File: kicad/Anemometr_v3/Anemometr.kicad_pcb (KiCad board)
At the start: 2 copper layers, 45 x 45 mm, 131 parts, among them J1 TxD, J10 +Z1, J11 +Z2, J12 +Z3, J13 +Z4, J14 -Z1, J15 -Z2, J16 -Z3, J17 -Z4, J2 RxD, J24 +Z1, J25 +Z1, J26 +Z1, J27 +Z1, J28 +Z1, J29 +Z1, J3 JST-SH1.0, J30 +Z1, J31 +Z1, J32 +Z1, J33 +Z1, J34 +Z1, J35 +Z1, J36 +Z1, J37 +Z1, J38 +Z1, J39 +Z1, J4 JST-SH1.0, J5 RST, J6 +EXT, J7 -EXT, J8 SWD, J9 SWC, Q1 5N10, U1 STM32F103C8Tx, U4 LMR14206, U6 NCP1117-3.3, U9 MCP1703-3.3, Y1 CSTCE8M00G52A-R0, Y2 ECS-250-20-33

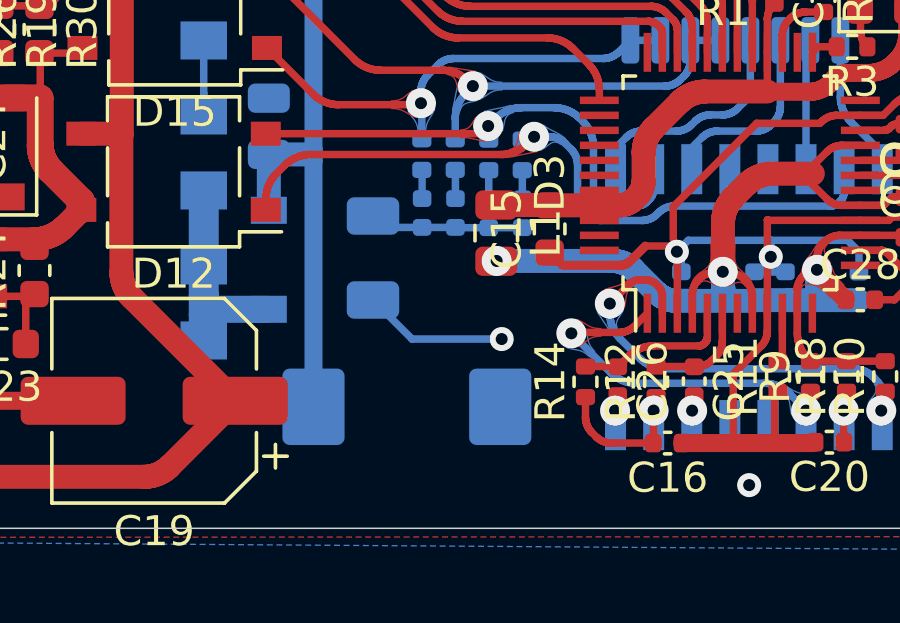
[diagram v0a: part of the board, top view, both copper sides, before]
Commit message: изменено:      kicad/Anemometr_v3/Anemometr.kicad_pcb 	изменено:      kicad/Anemometr_v3/Anemometr.kicad_pcb-bak 	изменено:      kicad/Anemometr_v3/Anemometr.sch 	изменено:      kicad/Anemometr_v3/Anemometr.sch-bak 	изменено:      kicad/Anemometr_v3/fp-info-cache 	удалено:       stm32cubeide/Anemometr_v3/Anemometr_3 Debug.launch 	изменено:      stm32cubeide/Anemometr_v3/Anemometr_3.ioc 	изменено:      stm32cubeide/Anemometr_v3/Core/Inc/main.h 	изменено:      stm32cubeide/Anemometr_v3/Core/Src/main.c 	изменено:      stm32cubeide/Anemometr_v3/Core/Src/stm32f1xx_it.c 	изменено:      stm32cubeide/Anemometr_v3/Core/Src/wizchip_conf.c 	изменено:      stm32cubeide/Anemometr_v3/Debug/Anemometr_3.bin 	удалено:       stm32cubeide/Anemometr_v3/Debug/Anemometr_3.elf 	изменено:      stm32cubeide/Anemometr_v3/Debug/Anemometr_3.map 	изменено:      stm32cubeide/Anemometr_v3/Debug/Core/Src/BME280.d 	изменено:      stm32cubeide/Anemometr_v3/Debug/Core/Src/BME280.o 	изменено:      stm32cubeide/Anemometr_v3/Debug/Core/Src/main.d 	изменено:      stm32cubeide/Anemometr_v3/Debug/Core/Src/main.o 	изменено:      stm32cubeide/Anemometr_v3/Debug/Core/Src/main.su 	изменено:      stm32cubeide/Anemometr_v3/Debug/Core/Src/stm32f1xx_hal_msp.d 	изменено:      stm32cubeide/Anemometr_v3/Debug/Core/Src/stm32f1xx_hal_msp.o 	изменено:      stm32cubeide/Anemometr_v3/Debug/Core/Src/stm32f1xx_it.d 	изменено:      stm32cubeide/Anemometr_v3/Debug/Core/Src/stm32f1xx_it.o 	изменено:      stm32cubeide/Anemometr_v3/Debug/Core/Src/wizchip_conf.o 	изменено:      stm32cubeide/Anemometr_v3/Release/Anemometr_3.bin 	изменено:      stm32cubeide/Anemometr_v3/Release/Anemometr_3.elf 	изменено:      stm32cubeide/Anemometr_v3/Release/Anemometr_3.hex 	изменено:      stm32cubeide/Anemometr_v3/Release/Anemometr_3.list 	изменено:      stm32cubeide/Anemometr_v3/Release/Anemometr_3.map 	изменено:      stm32cubeide/Anemometr_v3/Release/Core/Src/BME280.d 	изменено:      stm32cubeide/Anemometr_v3/Release/Core/Src/BME280.o 	изменено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
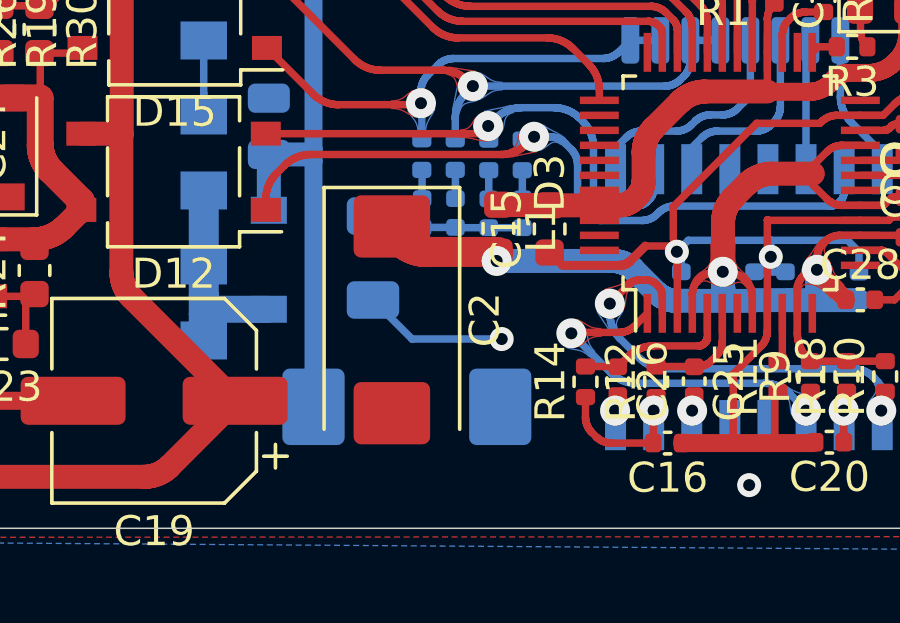
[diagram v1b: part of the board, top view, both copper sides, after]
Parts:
- added C2: 470uF x 6.3v, Capacitor_Tantalum_SMD:CP_EIA-7343-15_Kemet-W, F.Cu at (48.8, 80.5)
- L1: value 2.2uH -> HH-1M1608-121JT; footprint Inductor_SMD:L_0805_2012Metric -> Inductor_SMD:L_0603_1608Metric
- moved L1 0.18 mm to (52.3, 77.5)
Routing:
- net +3.3VA: track 40.9 -> 44.9 mm
